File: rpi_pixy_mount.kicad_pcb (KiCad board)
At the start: 2 copper layers, 65 x 56.5 mm, 26 parts, among them P1 RPi Connector, P2 Pixy Conn, P3 Power Input, P4 EEProm Write, Q1 BSS138, Q2 BSS138, Q3 BSS138, Q4 BSS138, Q5 BSS138, U1 CAT24C32WI-GT3

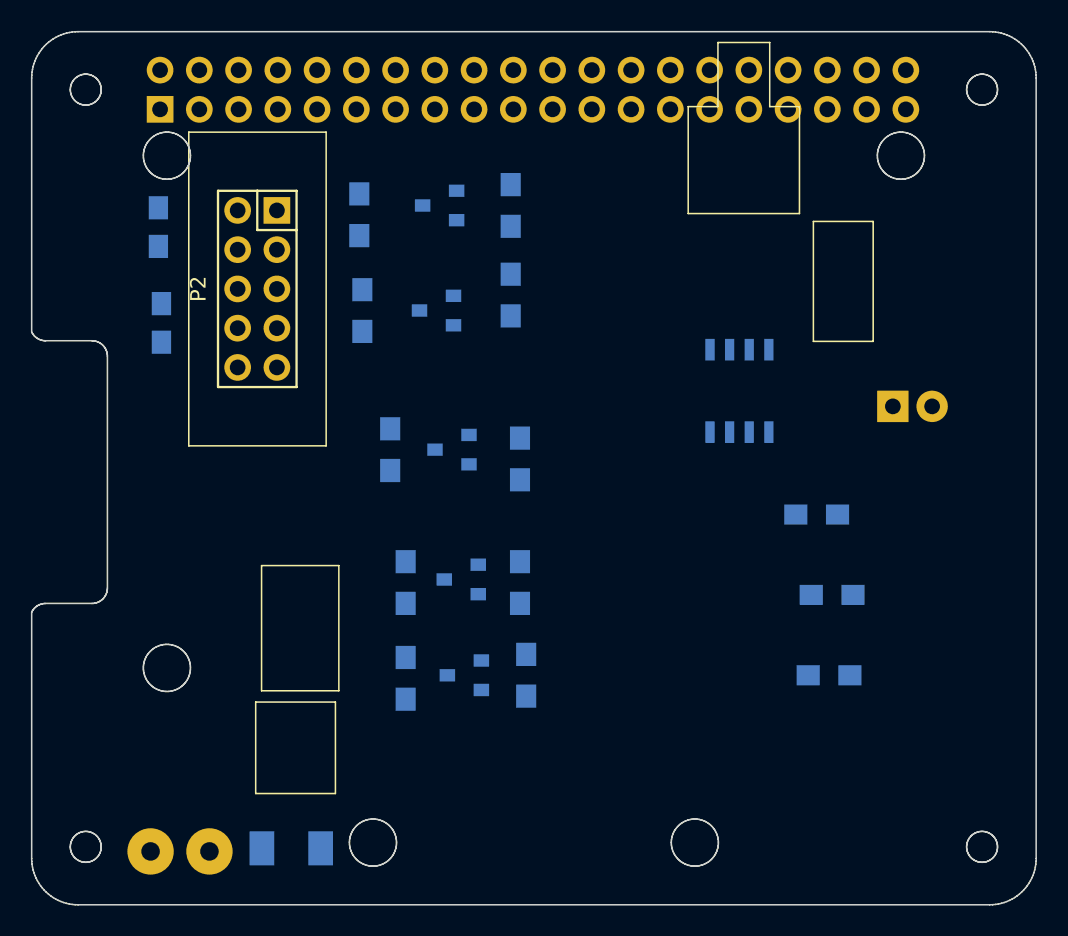
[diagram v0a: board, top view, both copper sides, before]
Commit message: Move mounting holes
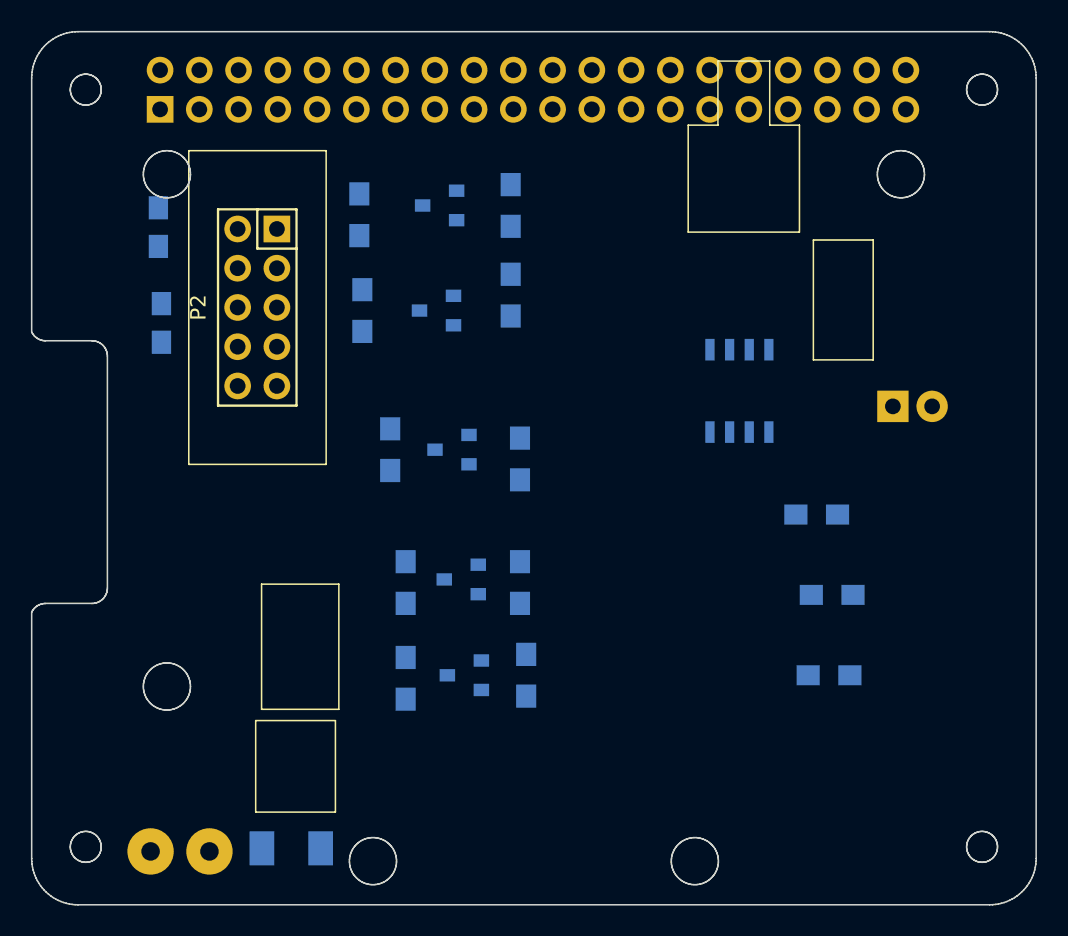
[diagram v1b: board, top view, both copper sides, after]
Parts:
- moved P2 1.20 mm to (130.6, 94.6)
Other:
- outline, holes or cut-outs redrawn
